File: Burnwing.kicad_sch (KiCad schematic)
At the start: 52 parts, among them J1 Conn_01x03_Pin, J2 USB Type C, J3 Conn_01x02_Pin, J5 Conn_01x06_MountingPin-Mirror, J6 Conn_01x06_MountingPin, Q1 AONR21307, SW1 SW_DIP_x02, U1 HUSB238, U2 BTS7030-2EPA, U3 TPS70933QDBVRQ1

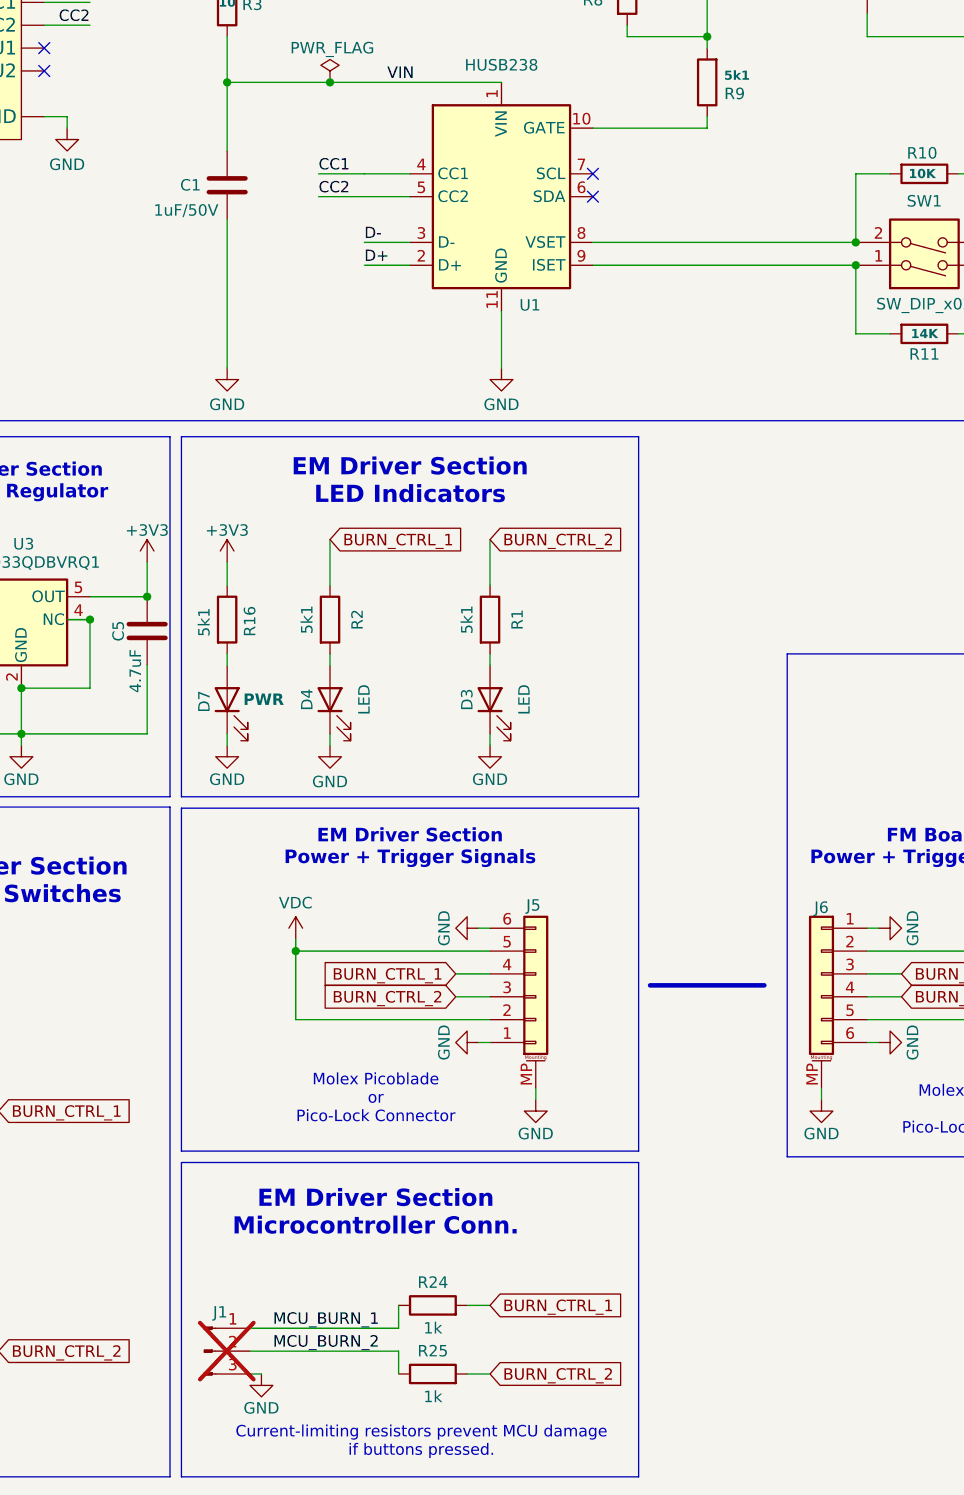
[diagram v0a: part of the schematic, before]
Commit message: Self-contained libraries, Rev 3.0 renders, README
Move footprint/symbol assignments into the project-local Burnwing.pretty
and Burnwing.kicad_sym libraries so the project builds without external
library dependencies. Adds PinSocket 1x02/1x04 and the DB128L-5.08-2P
screw terminal (symbol, footprint and 3D model).

Add top and bottom renders of Rev 3.0 and reference them from the README,
replacing the stale docs/Render_Top.png link.

Ignore .history_trim/ and internal PCB review reports.
Claude-Session: https://claude.ai/code/session_01PXHPcjwL7EimSN7b4jQgcZ
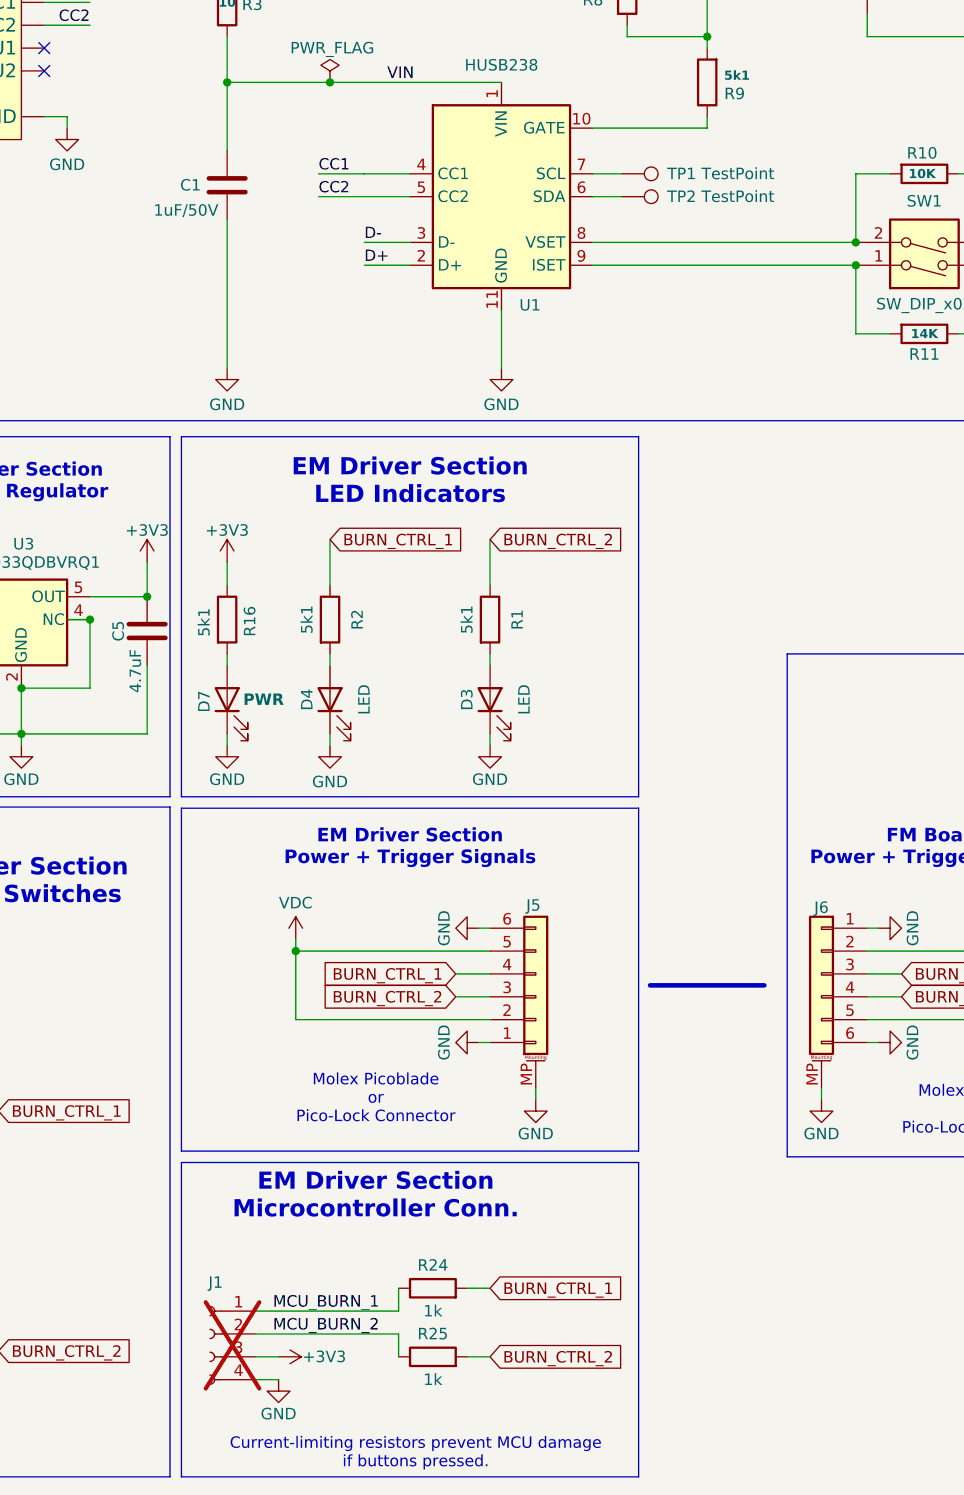
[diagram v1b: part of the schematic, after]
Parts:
- added TP1, TP2: TestPoint, symbol Burnwing:TestPoint
- C1, C2, C3, C4, C5: symbol Device:C -> Burnwing:C
- D3, D4, D7: symbol Device:LED -> Burnwing:LED
- H1, H2, H3, H4, H5, H6, H7, H8: symbol Mechanical:MountingHole_Pad -> Burnwing:MountingHole_Pad
- J1: value Conn_01x03_Pin -> Conn_01x04_Socket; footprint Connector_PinHeader_2.54mm:PinHeader_1x03_P2.54mm_Vertical -> Connector_PinSocket_2.54mm:PinSocket_1x04_P2.54mm_Vertical; symbol Connector:Conn_01x03_Pin -> Burnwing:Conn_01x04_Socket; now in the parts list
- J3: footprint (none) -> Connector_PinSocket_1.27mm:PinSocket_1x02_P1.27mm_Vertical; symbol Connector:Conn_01x02_Pin -> Burnwing:Conn_01x02_Pin
- J5: symbol Connector_Generic_MountingPin:Conn_01x06_MountingPin -> Burnwing:Conn_01x06_MountingPin_1
- J6: symbol Connector_Generic_MountingPin:Conn_01x06_MountingPin -> Burnwing:Conn_01x06_MountingPin
- R1, R10, R11, R12, R13, R14, R16, R17, R18, R19, R2, R21, R22, R23, R24, R25, R26, R27, R28, R29, R3, R30, R8, R9: symbol Device:R -> Burnwing:R
- SW1: symbol Switch:SW_DIP_x02 -> Burnwing:SW_DIP_x02
- U1: symbol Interface_USB:HUSB238_xxxDD -> Burnwing:HUSB238_xxxDD
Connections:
- net +3V3: now also J1.3 (Pin_3)
- net GND: now also J1.4 (Pin_4); no longer J1.3 (Pin_3)
- net at U1.6 (SDA): now also TP2.1
- net at U1.7 (SCL): now also TP1.1
- no-connect marks 5 -> 3
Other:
- title: Burnwing Eng. -> Burnwing
- moved on the sheet: R24, R25

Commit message: Layout complete - Ready for review
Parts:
- removed Burn1, Burn2: KEY-SMD_4P-L6.0-W6.0-P4.50-LS9.5-BR, Burnwing:KEY-SMD_4P-L6.0-W6.0-P4.50-LS9.5-BR, symbol Burnwing:Tactile_Button
- removed TP1, TP2: TestPoint, symbol Burnwing:TestPoint
- added Burn1, Burn2: TSA063G43-250, EasyEDA:KEY-SMD_4P-L6.0-W6.0-P4.50-LS10.0, symbol Burnwing:TSA063G43-250
- added C6: 4.7uF, Burnwing:C_0805_2012Metric_Pad1.18x1.45mm_HandSolder, symbol Burnwing:C
- added J4: Conn_01x02_Pin, Burnwing:PinSocket_1x02_P1.27mm_Vertical, symbol Burnwing:Conn_01x02_Pin
- added R20, R31: 100k, Burnwing:R_0603_1608Metric_Pad0.98x0.95mm_HandSolder, symbol Burnwing:R
- C1, C2, C3, C4, C5: footprint Capacitor_SMD:C_0805_2012Metric_Pad1.18x1.45mm_HandSolder -> Burnwing:C_0805_2012Metric_Pad1.18x1.45mm_HandSolder
- D3, D4, D7: footprint LED_SMD:LED_0603_1608Metric_Pad1.05x0.95mm_HandSolder -> Burnwing:LED_0603_1608Metric_Pad1.05x0.95mm_HandSolder
- H1, H2, H3, H4, H5, H6, H7, H8: footprint MountingHole:MountingHole_2.2mm_M2_Pad -> Burnwing:MountingHole_2.2mm_M2_Pad
- J1: footprint Connector_PinSocket_2.54mm:PinSocket_1x04_P2.54mm_Vertical -> Burnwing:HDR-TH_4P-P2.54-V-F; now left out of the parts list
- J3: footprint Connector_PinSocket_1.27mm:PinSocket_1x02_P1.27mm_Vertical -> Burnwing:PinSocket_1x02_P1.27mm_Vertical; now not fitted; now left out of the parts list
- J5: footprint Burnwing:Molex_Pico-Lock_and_PicoBlade -> Burnwing:Molex_Pico-Lock_and_PicoBlade2
- R1, R10, R11, R14, R16, R17, R18, R19, R2, R21, R22, R23, R24, R25, R26, R27, R28, R29, R3, R30, R8, R9: footprint Resistor_SMD:R_0603_1608Metric_Pad0.98x0.95mm_HandSolder -> Burnwing:R_0603_1608Metric_Pad0.98x0.95mm_HandSolder
- U1: footprint Package_DFN_QFN:WDFN-10-1EP_3x3mm_P0.5mm_EP1.8x2.5mm -> Burnwing:WDFN-10-1EP_3x3mm_P0.5mm_EP1.8x2.5mm
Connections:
- net +3V3: now also Burn1.1, Burn1.2, Burn2.1, Burn2.2
- net BURN_CTRL_1: now also Burn1.3, Burn1.4
- net BURN_CTRL_2: now also Burn2.3, Burn2.4
- net GND: now also C6.2, R31.2
- net VDC: now also C6.1, R20.1
- net at J3.1 (Pin_1), U3.3 (EN): now also R20.2, R31.1
- net at U1.6 (SDA): now also J4.2 (Pin_2)
- net at U1.7 (SCL): now also J4.1 (Pin_1)
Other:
- note added: "Backup Pullup"
- note added: "Disable Pulldown"
- note added: "Unconnected EN Enabled"
- moved on the sheet: C4, C5, D3, D4, D7, J1, J5, R1, R16, R2, R24, R25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

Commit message: Cleaning up files
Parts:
- Burn1, Burn2: footprint EasyEDA:KEY-SMD_4P-L6.0-W6.0-P4.50-LS10.0 -> Burnwing:KEY-SMD_4P-L6.0-W6.0-P4.50-LS10.0
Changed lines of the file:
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@@
 		(dnp no)
 		(property "Reference" "Burn2"
-			(at 26.67 179.705 0)
+			(at 26.67 179.07 0)
 			(show_name no)
 			(do_not_autoplace no)
@@
 			)
 		)
-		(property "Footprint" "EasyEDA:KEY-SMD_4P-L6.0-W6.0-P4.50-LS10.0"
+		(property "Footprint" "Burnwing:KEY-SMD_4P-L6.0-W6.0-P4.50-LS10.0"
 			(at 26.67 194.31 0)
 			(hide yes)
@@
 		(dnp no)
 		(property "Reference" "Burn1"
-			(at 26.67 153.035 0)
+			(at 26.67 152.4 0)
 			(show_name no)
 			(do_not_autoplace no)
@@
 			)
 		)
-		(property "Footprint" "EasyEDA:KEY-SMD_4P-L6.0-W6.0-P4.50-LS10.0"
+		(property "Footprint" "Burnwing:KEY-SMD_4P-L6.0-W6.0-P4.50-LS10.0"
 			(at 26.67 167.64 0)
 			(hide yes)

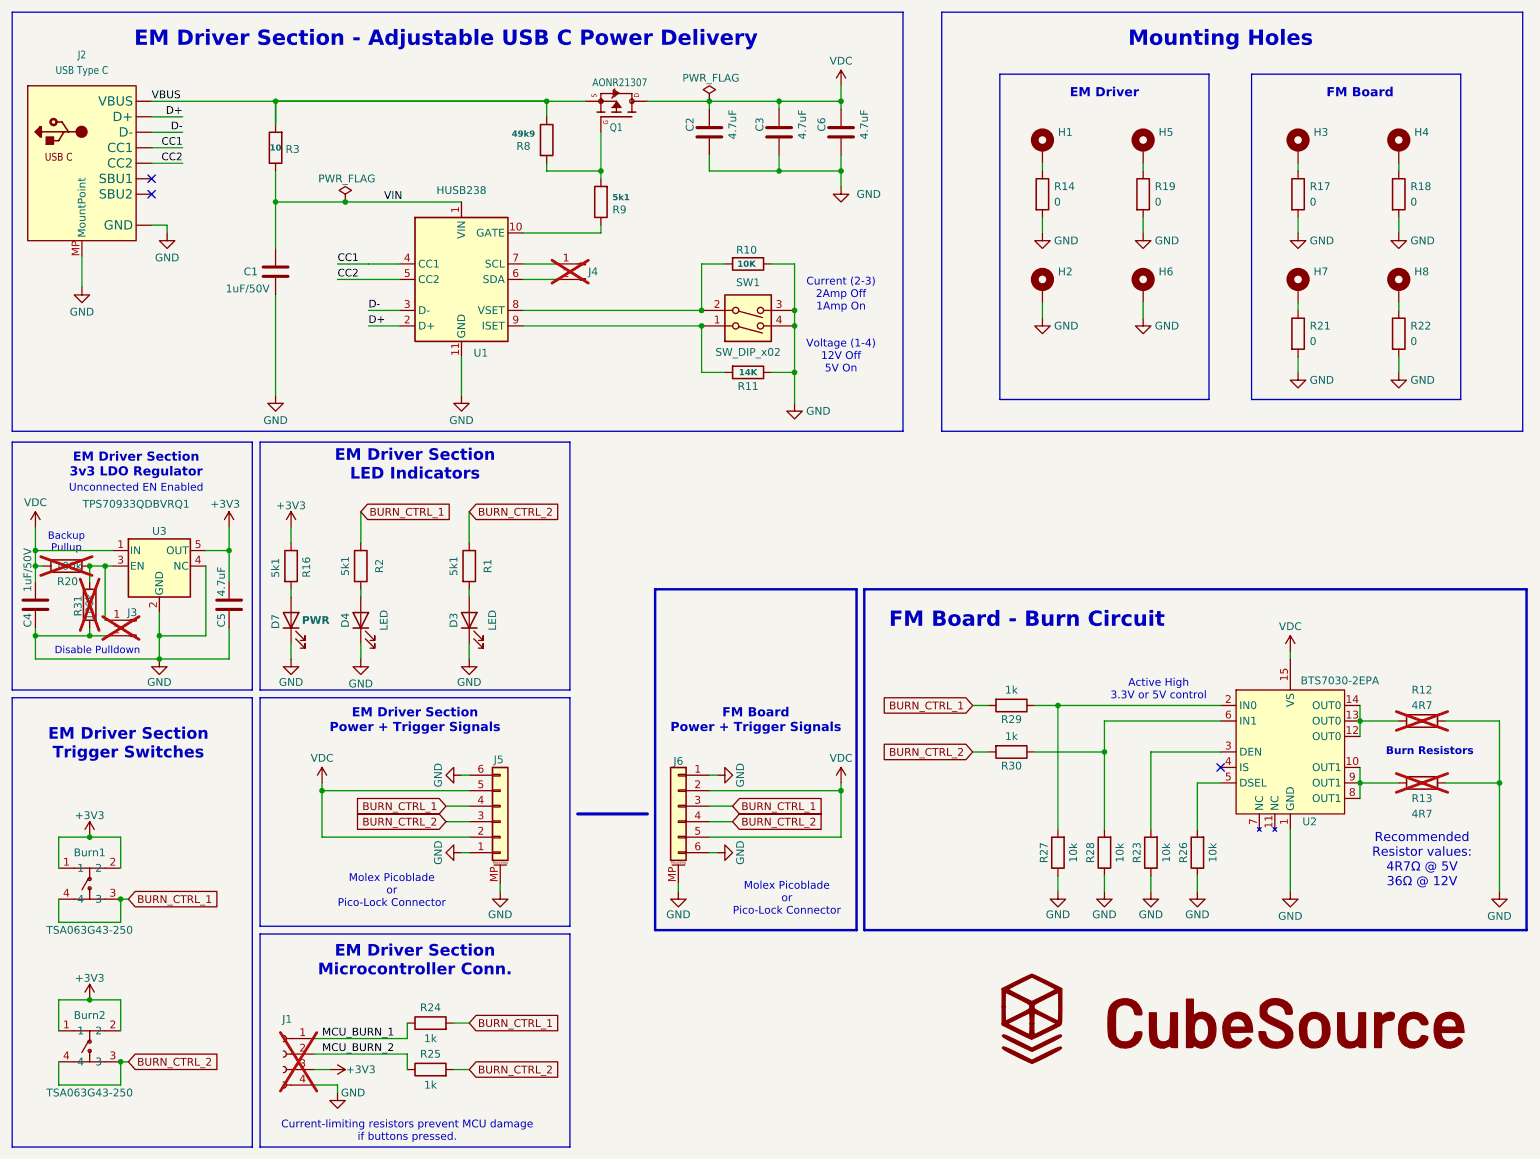
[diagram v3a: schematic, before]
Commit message: Add Pico-Lock connector part, teardrops, and panel break tabs
Schematic:
- Add local 5040500691 symbol (Molex Pico-Lock 504050-0691) with datasheet
- Add R32 (47R 0603); retarget R27 to the local Burnwing:R symbol
- Switch the 6-pin connector from the mirrored footprint variant to the
  standard Molex_Pico-Lock_and_PicoBlade

PCB:
- Apply teardrops to pads and vias (13 -> 155 zones)
- Rework routing: 180 -> 252 track segments, 73 -> 66 vias
- Rework the panel edge: add four BreakLine_1h_D0.5mm_P0.85mm tabs,
  drop one mouse bite

Libraries:
- Add CONN-SMD_6P-P1.50_A1501WRB-S-6P footprint with STEP/WRL models
- Rename Molex_Pico-Lock_and_PicoBlade2 to Molex_Pico-Lock_and_PicoBlade_Mirror
- Add BreakLine_1h_D0.5mm_P0.85mm footprint

Library path cleanup:
- fp-lib-table: repoint Burnwing from the machine-local ${EASY} to
  ${KIPRJMOD}, and drop the bogus duplicate Burnwing.pretty entry that
  pointed at a non-existent directory
- sym-lib-table: drop the stale EasyEDA entry (file never existed)
- Consolidate 3D models into packages3D/, matching the existing convention,
  and remove the parallel Burnwing.3dshapes/ directory
- Repoint the two Molex footprints off an absolute ${DOWNLOADS} path and
  CONN-SMD_6P off ${KICAD_3RD_PARTY}; all 3D model references now resolve
- Fix stale footprint library nicknames on the TSA063G43-250 and
  Conn_01x06_MountingPin-Mirror symbols (EasyEDA:/00-Project-Footprint-Lib:
  -> Burnwing:), and sync the schematic's cached symbol copy to match
- Delete the stray importer-generated Burnwing.pretty.kicad_sym

Board setup:
- Zone defaults: 1mm corner radius, smoothing enabled, 0.2mm min clearance
- Clear four stale "Internally Connected" DRC exclusions

ERC is unchanged by the path cleanup (1 pre-existing power_pin_not_driven
on U2 pin 1); HEAD's "Molex_Pico-Lock_and_PicoBlade2 not found" warning is
resolved.
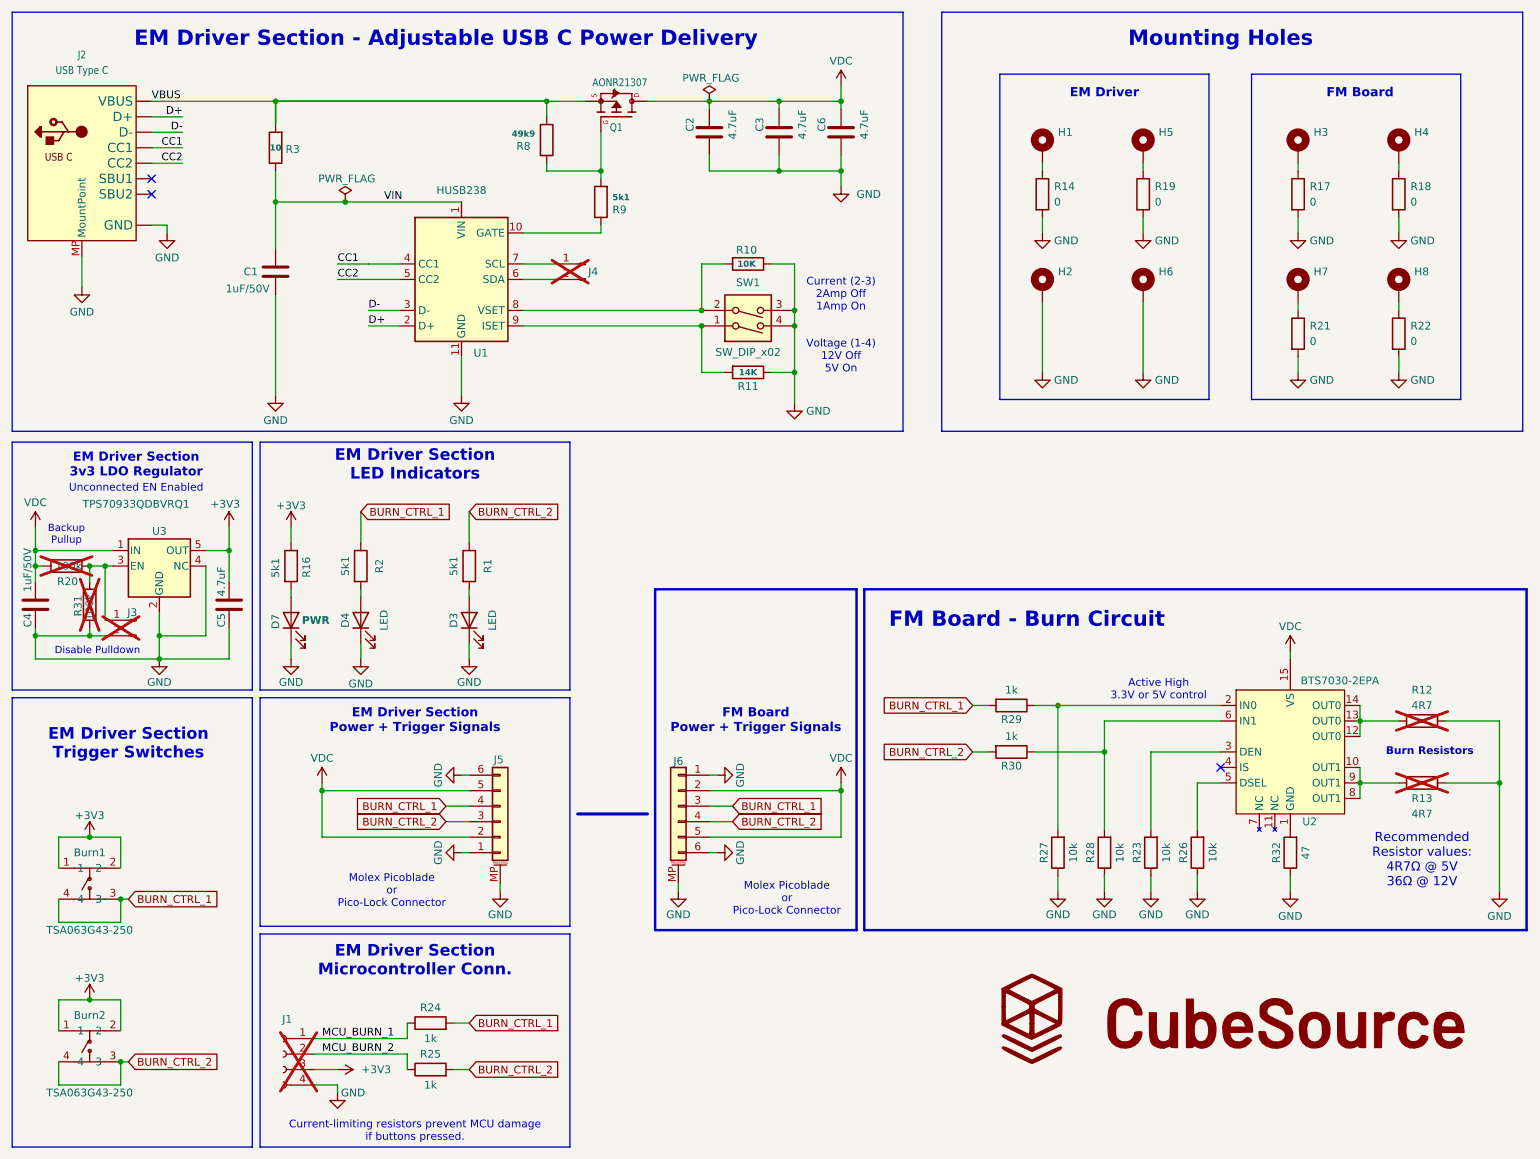
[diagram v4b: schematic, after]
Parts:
- added R32: 47, Burnwing:R_0603_1608Metric_Pad0.98x0.95mm_HandSolder, symbol Burnwing:R
- J5: value Conn_01x06_MountingPin-Mirror -> Conn_01x06_MountingPin; footprint Burnwing:Molex_Pico-Lock_and_PicoBlade2 -> Burnwing:Molex_Pico-Lock_and_PicoBlade
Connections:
- net GND: now also R32.1; no longer U2.1 (GND)
- new net: R32.2, U2.1 (GND)
